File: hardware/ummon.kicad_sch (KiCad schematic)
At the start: 95 parts, among them J1 Conn_01x08_Pin, J2 Conn_01x05_Pin, J3 Conn_01x04_Pin, J4 Conn_01x04_Pin, J5 Conn_01x04_Pin, P1 FPC 0.5MM 24P Vertical, Q1 SI1308EDL, SW1 Reboot, SW2 Flash, SW3 Test Button, SW4 MINI MSK12CO2, U1 ESP32-C6-WROOM-1-N8, U2 SCD41-D-R2, U3 SGP41-D-R4, U4 SHT41-AD1B-R2, U5 AMS1117-3.3

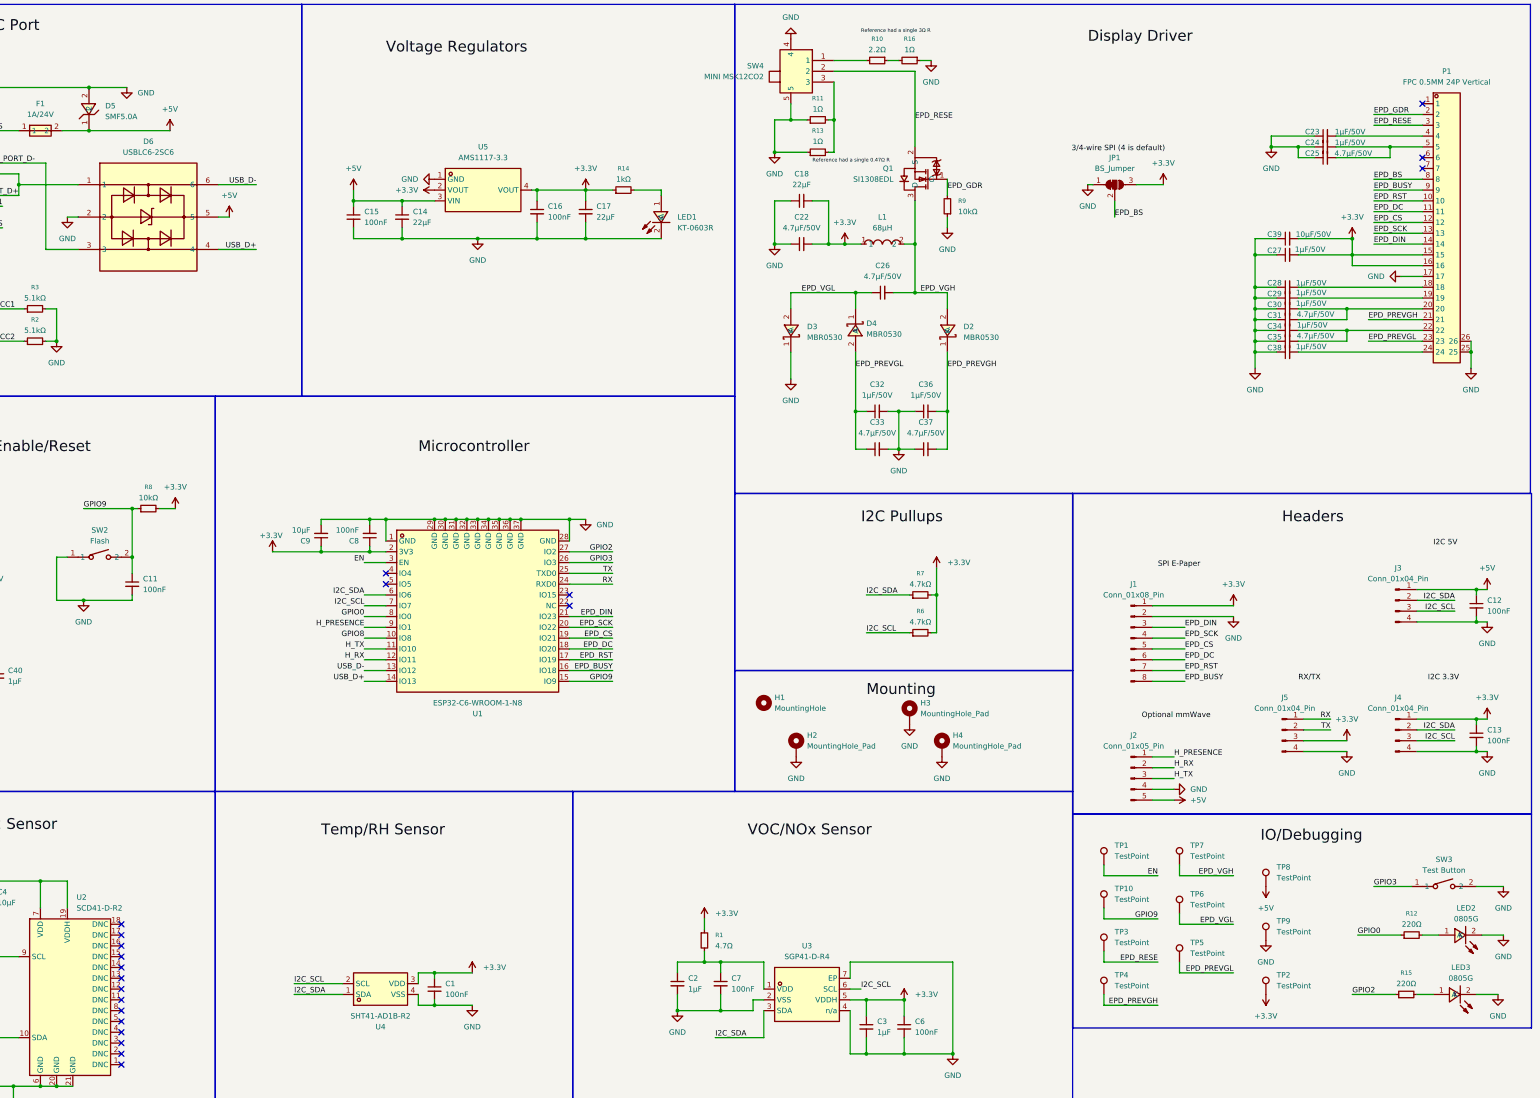
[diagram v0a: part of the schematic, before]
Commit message: :recycle: Name testpoints and move part of 3V3 to inner layer
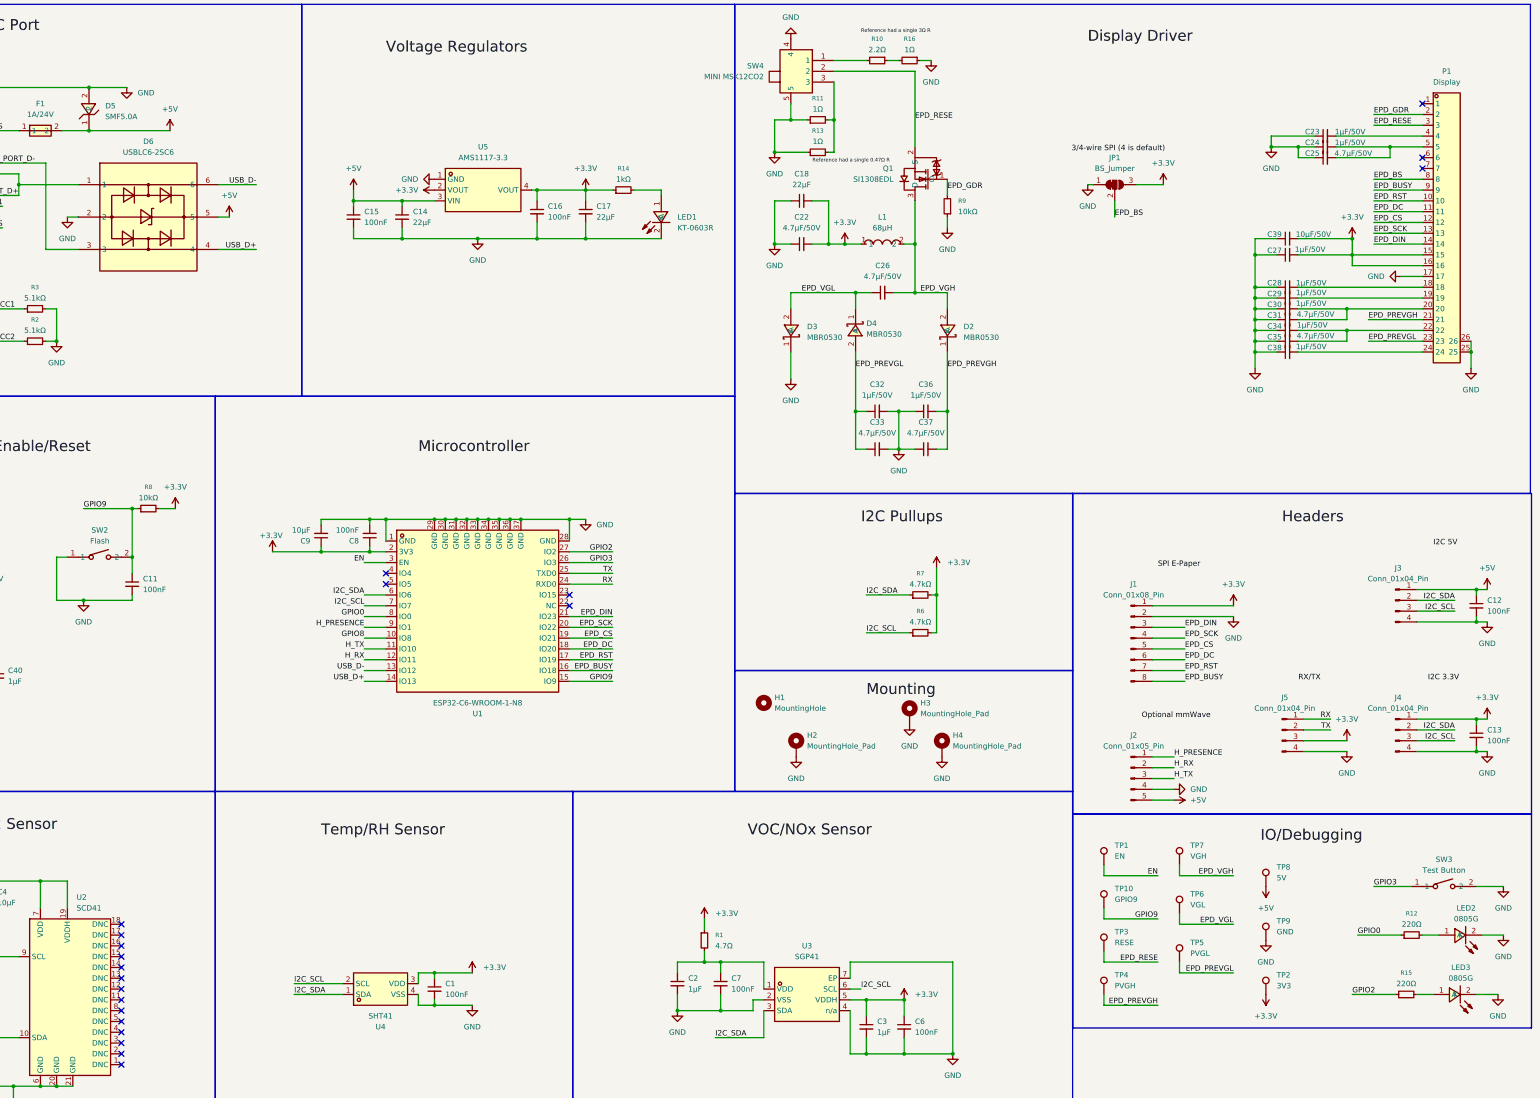
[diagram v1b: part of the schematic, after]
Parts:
- P1: value FPC 0.5MM 24P Vertical -> Display
- TP1: value TestPoint -> EN
- TP10: value TestPoint -> GPIO9
- TP2: value TestPoint -> 3V3
- TP3: value TestPoint -> RESE
- TP4: value TestPoint -> PVGH
- TP5: value TestPoint -> PVGL
- TP6: value TestPoint -> VGL
- TP7: value TestPoint -> VGH
- TP8: value TestPoint -> 5V
- TP9: value TestPoint -> GND
- U2: value SCD41-D-R2 -> SCD41
- U3: value SGP41-D-R4 -> SGP41
- U4: value SHT41-AD1B-R2 -> SHT41
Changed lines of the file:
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@@
 			)
 		)
-		(property "Value" "SGP41-D-R4"
+		(property "Value" "SGP41"
 			(at 237.49 236.22 0)
 			(show_name no)
@@
 			)
 		)
-		(property "Value" "SCD41-D-R2"
+		(property "Value" "SCD41"
 			(at 65.6433 224.79 0)
 			(show_name no)
@@
 			)
 		)
-		(property "Value" "TestPoint"
+		(property "Value" "PVGL"
 			(at 327.66 235.4579 0)
 			(show_name no)
@@
 			)
 		)
-		(property "Value" "TestPoint"
+		(property "Value" "EN"
 			(at 309.88 212.5979 0)
 			(show_name no)
@@
 			)
 		)
-		(property "Value" "TestPoint"
+		(property "Value" "5V"
 			(at 347.98 217.6779 0)
 			(show_name no)
@@
 			)
 		)
-		(property "Value" "TestPoint"
+		(property "Value" "PVGH"
 			(at 309.88 243.0779 0)
 			(show_name no)
@@
 			)
 		)
-		(property "Value" "TestPoint"
+		(property "Value" "RESE"
 			(at 309.88 232.9179 0)
 			(show_name no)
@@
 			)
 		)
-		(property "Value" "TestPoint"
+		(property "Value" "GPIO9"
 			(at 309.88 222.7579 0)
 			(show_name no)
@@
 			)
 		)
-		(property "Value" "TestPoint"
+		(property "Value" "VGH"
 			(at 327.66 212.5979 0)
 			(show_name no)
@@
 			)
 		)
-		(property "Value" "TestPoint"
+		(property "Value" "GND"
 			(at 347.98 230.3779 0)
 			(show_name no)
@@
 			)
 		)
-		(property "Value" "TestPoint"
+		(property "Value" "VGL"
 			(at 327.66 224.0279 0)
 			(show_name no)
@@
 			)
 		)
-		(property "Value" "FPC 0.5MM 24P Vertical"
+		(property "Value" "Display"
 			(at 387.985 30.48 0)
 			(show_name no)
@@
 			)
 		)
-		(property "Value" "SHT41-AD1B-R2"
+		(property "Value" "SHT41"
 			(at 137.16 250.19 0)
 			(show_name no)
@@
 			)
 		)
-		(property "Value" "TestPoint"
+		(property "Value" "3V3"
 			(at 347.98 243.0779 0)
 			(show_name no)

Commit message: :construction: WIP reverse display pinout and unplace epd section
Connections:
- net +3.3V: now also P1.10, P1.9; no longer P1.15, P1.16
- net EPD_BS: now also P1.17; no longer P1.8
- net EPD_BUSY: now also P1.16, U1.21 (IO23); no longer P1.9, U1.16 (IO18)
- net EPD_CS: now also P1.13, U1.18 (IO20); no longer P1.12, U1.19 (IO21)
- net EPD_DC: now also P1.14, U1.19 (IO21); no longer P1.11, U1.18 (IO20)
- net EPD_DIN: now also P1.11, U1.16 (IO18); no longer P1.14, U1.21 (IO23)
- net EPD_GDR: now also P1.23; no longer P1.2
- net EPD_PREVGH: now also P1.4; no longer P1.21
- net EPD_PREVGL: now also P1.2; no longer P1.23
- net EPD_RESE: now also P1.22; no longer P1.3
- net EPD_RST: now also P1.15, U1.20 (IO22); no longer P1.10, U1.17 (IO19)
- net EPD_SCK: now also P1.12, U1.17 (IO19); no longer P1.13, U1.20 (IO22)
- net GND: now also P1.8; no longer P1.17, P1.25, P1.26
- net at C34.2, C35.2: now also P1.3; no longer P1.22
- net at C30.2, C31.2: now also P1.5; no longer P1.20
- net at C28.2: now also P1.7; no longer P1.18
- net at C24.2, C25.2: now also P1.20; no longer P1.5
- net at P1.1: now also C38.2
- net at P1.19: no longer C29.2
- net at P1.24: no longer C38.2
- net at C23.2: now also P1.21; no longer P1.4
- net at P1.6: now also C29.2
- no-connect marks 23 -> 25
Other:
- moved on the sheet: C23, C24, C25, C27, C28, C29, C30, C31, C34, C35, C38, C39

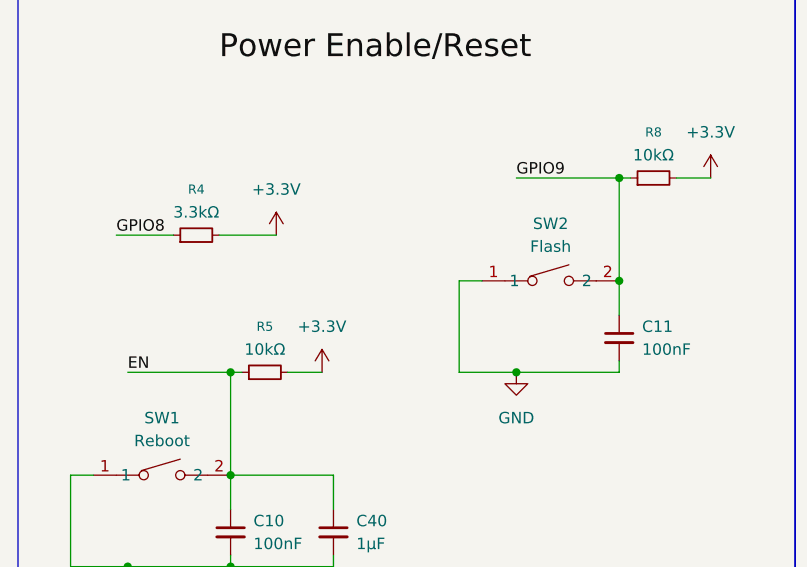
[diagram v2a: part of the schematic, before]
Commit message: :sparkles: Completes routing after connector flip
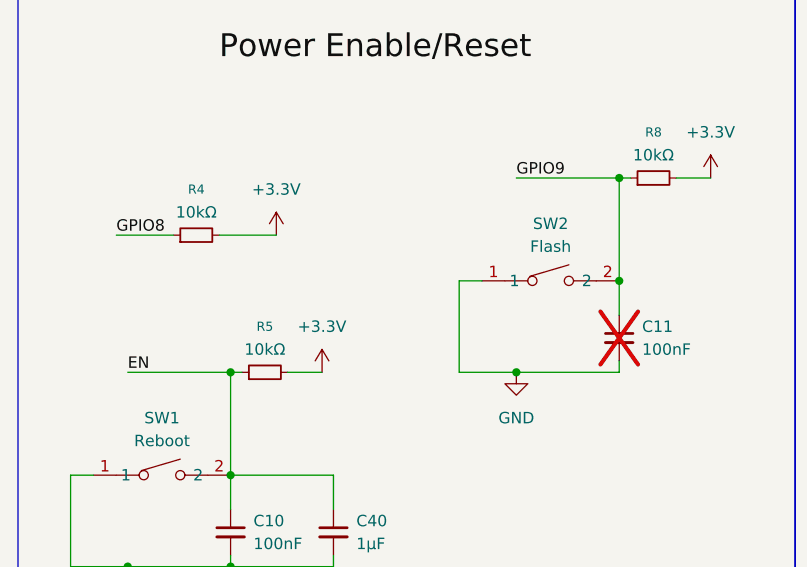
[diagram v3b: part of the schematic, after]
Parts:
- C11: now not fitted
- R4: value 3.3kΩ -> 10kΩ; LCSC Part C26010 -> C17414
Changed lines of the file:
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@@
 			)
 		)
-		(property "Value" "3.3kΩ"
+		(property "Value" "10kΩ"
 			(at 31.75 134.62 90)
 			(show_name no)
@@
 			)
 		)
-		(property "LCSC Part" "C26010"
+		(property "LCSC Part" "C17414"
 			(at 31.75 137.16 90)
 			(hide yes)
@@
 		(on_board yes)
 		(in_pos_files yes)
-		(dnp no)
+		(dnp yes)
 		(fields_autoplaced yes)
 		(property "Reference" "C11"

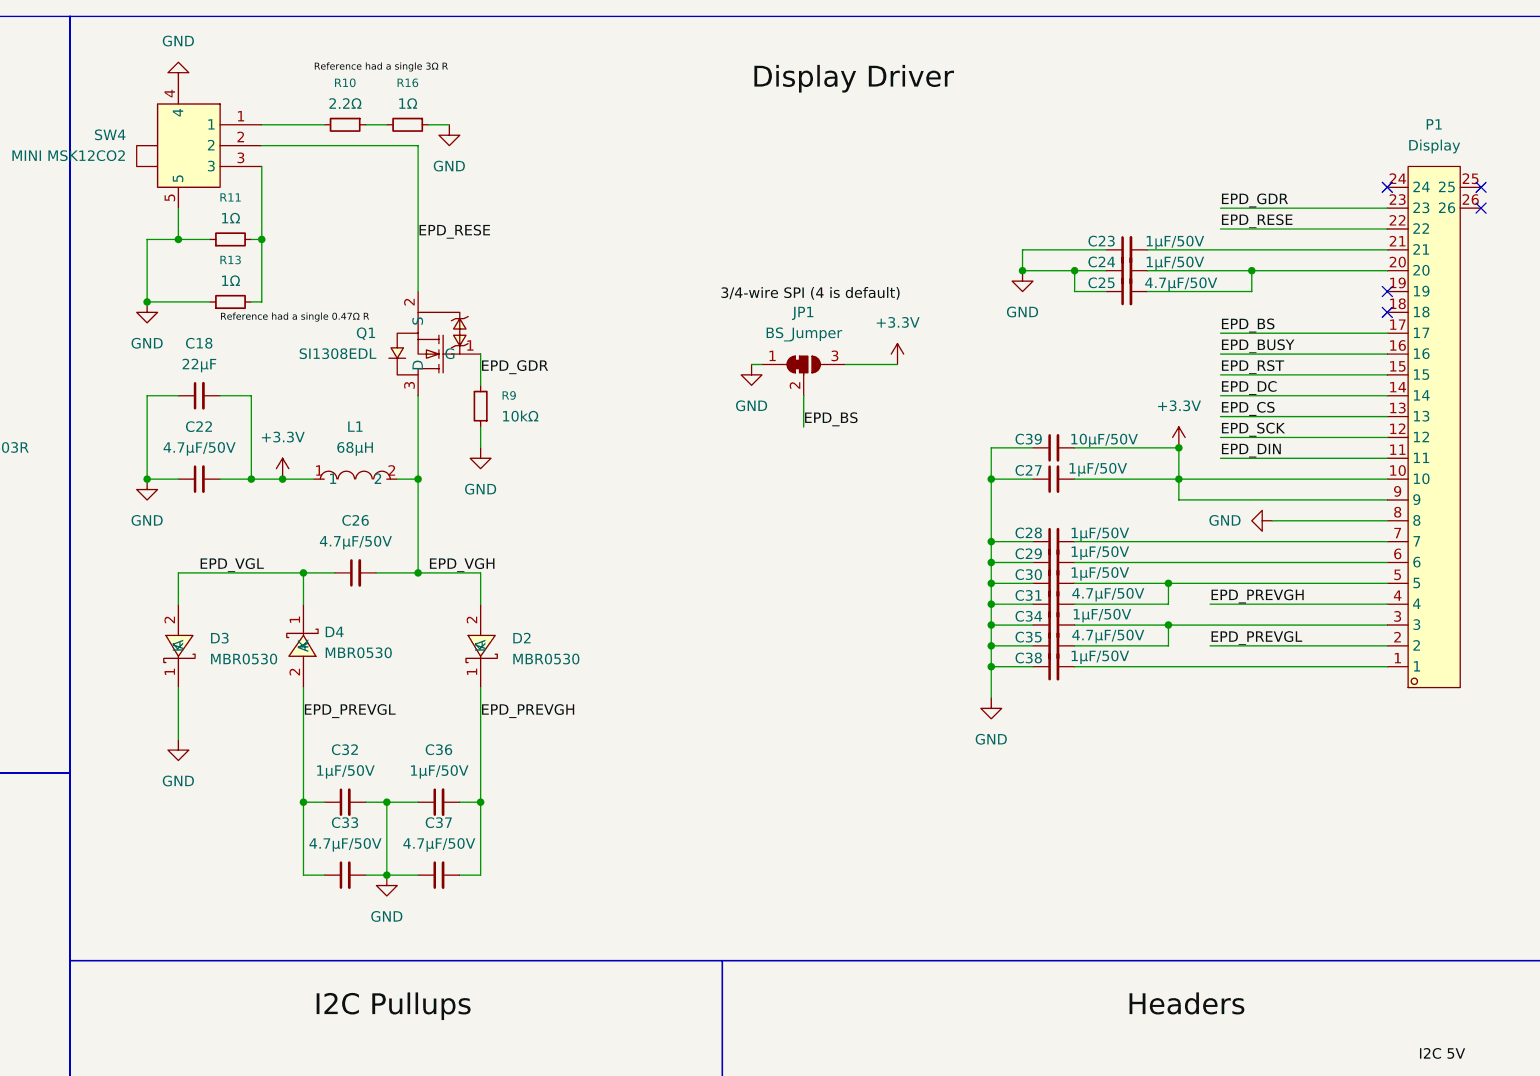
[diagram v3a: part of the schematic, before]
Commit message: :construction: WIP refactor driver hat to version 2.3
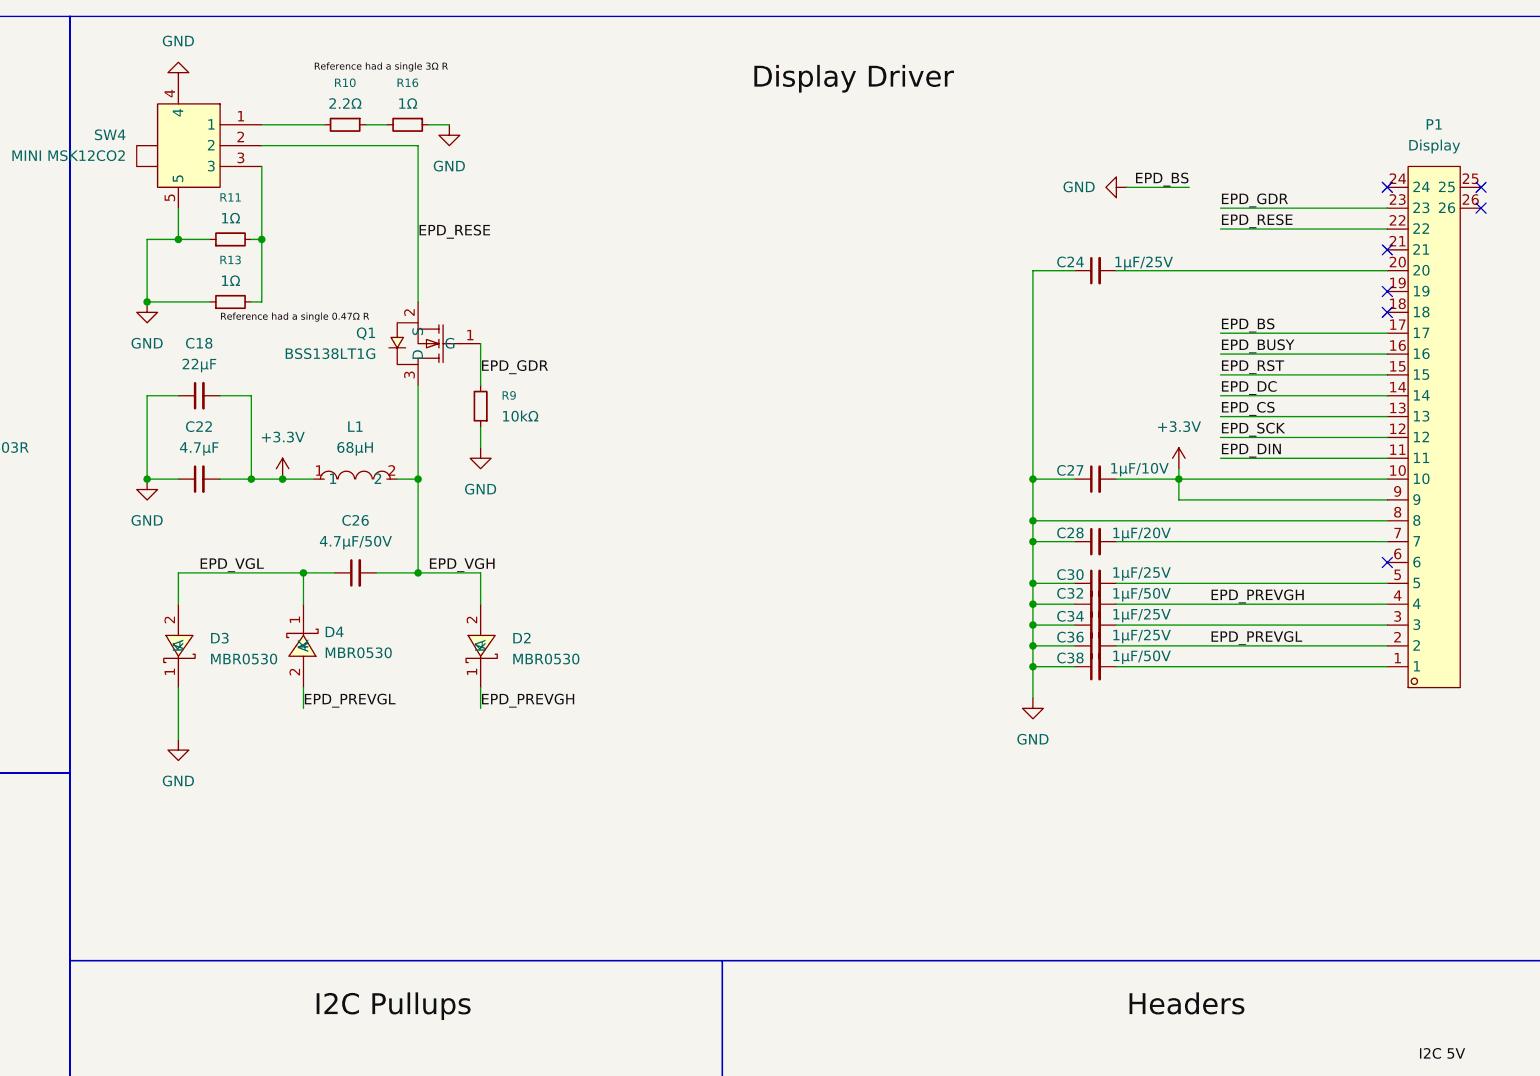
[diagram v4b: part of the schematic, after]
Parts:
- removed C23, C29: 1μF/50V, Capacitor_SMD:C_0805_2012Metric, symbol Device:C_Small
- removed C25, C31, C33, C35, C37: 4.7μF/50V, Capacitor_SMD:C_1206_3216Metric, symbol Device:C_Small
- removed C39: 10μF/50V, Capacitor_SMD:C_0805_2012Metric, symbol Device:C_Small
- removed JP1: BS_Jumper, Jumper:SolderJumper-3_P1.3mm_Bridged12_RoundedPad1.0x1.5mm_NumberLabels, symbol Jumper:SolderJumper_3_Bridged12
- removed Q1: SI1308EDL, parts:SOT-323_L2.0-W1.3-P1.30-LS2.1-BR, symbol parts:SI1308EDL-T1-GE3
- added Q1: BSS138LT1G, parts:SOT-23-3_L2.9-W1.6-P1.90-LS2.8-BR, symbol parts:BSS138LT1G
- C22: value 4.7μF/50V -> 4.7μF
- C24, C30, C34, C36: value 1μF/50V -> 1μF/25V
- C27: value 1μF/50V -> 1μF/10V
- C28: value 1μF/50V -> 1μF/20V
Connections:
- net EPD_BS is gone; now on net GND: P1.17
- net EPD_GDR: now also Q1.1 (G)
- net EPD_PREVGH: now also C32.2; no longer C36.2
- net EPD_PREVGL: now also C36.2; no longer C32.1
- net EPD_RESE: now also Q1.2 (S)
- net EPD_VGH: now also Q1.3 (D)
- net GND: now also C32.1; no longer C32.2
- no-connect marks 25 -> 27
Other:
- moved on the sheet: C24, C27, C28, C30, C32, C34, C36, C38
